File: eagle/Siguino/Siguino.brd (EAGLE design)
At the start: 71 x 39 mm, 47 parts, among them J1 FTDI, J4 10118193-0001LF, Q1 MOSFET P-CH 20V 5.3A SOT-23, U1 ATMEGA328P_TQFP, U2 LIS3MDLTR_LIS3MDLTR, U3 SPARKFUN-SENSORS_LIS3DH, U4 BME280, U5 FT232RL, U6 MAX1724EZK33+T, Y1 8MHz

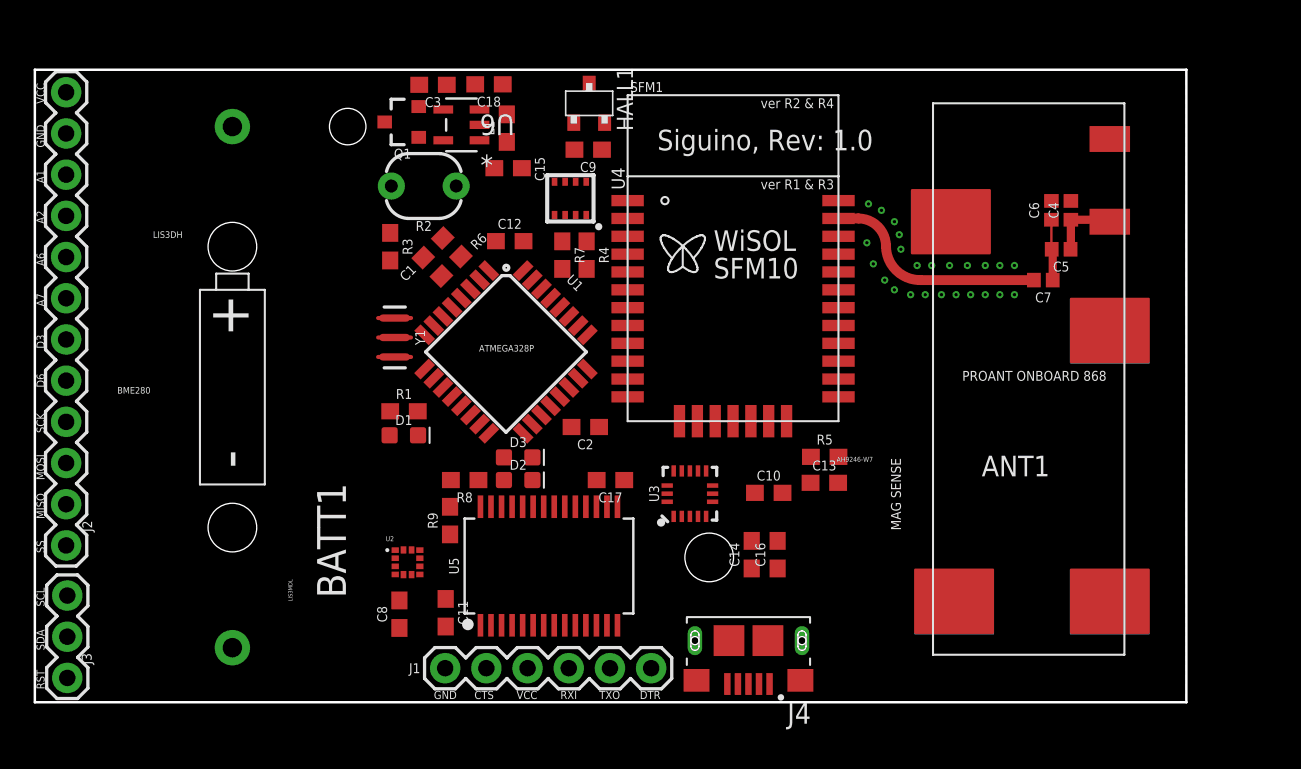
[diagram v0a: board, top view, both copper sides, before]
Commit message: Re-routed board, unfinished
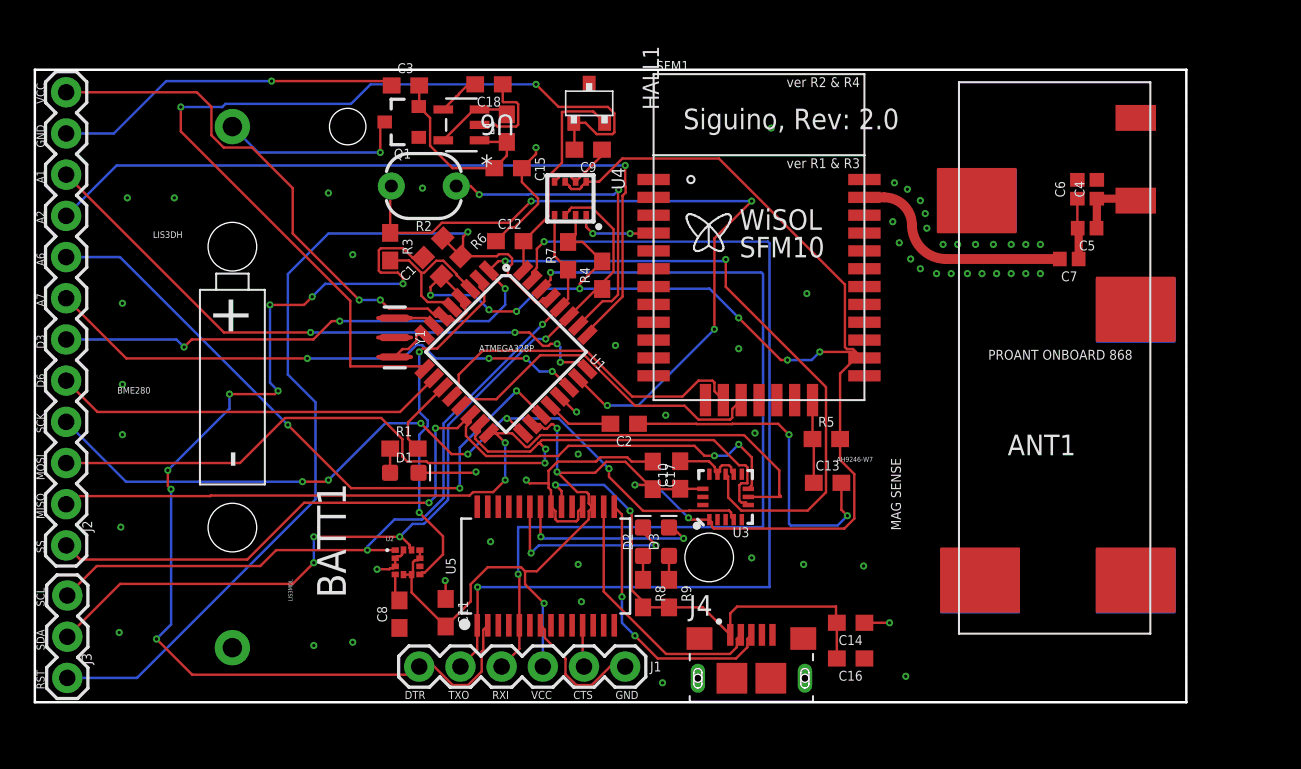
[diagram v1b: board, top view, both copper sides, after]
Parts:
- moved J1 14.3 mm to (23.7, 2.20), turned to 0 degrees
- moved R9 14.2 mm to (39.1, 6.70), turned to 270 degrees
- moved R8 13.0 mm to (37.5, 6.70), turned to 270 degrees
- moved D3 10.7 mm to (39.1, 9.90), turned to 90 degrees
- moved D2 8.59 mm to (37.5, 9.90), turned to 90 degrees
- moved C16 7.82 mm to (50.3, 2.70), turned to 180 degrees
- moved C14 7.41 mm to (50.3, 4.90), turned to 180 degrees
- moved C10 5.57 mm to (39.8, 14.0), turned to 90 degrees
- moved C17 2.63 mm to (38.1, 14.0), turned to 270 degrees
- moved C2 2.41 mm to (36.3, 17.2)
- moved J4 2.33 mm to (44.2, 1.48), turned to 0 degrees
- moved D1 2.31 mm to (22.8, 14.2)
- moved R1 2.30 mm to (22.8, 15.6)
- moved U3 2.21 mm to (42.6, 12.7)
- moved ANT1 2.06 mm to (62.9, 21.2)
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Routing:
- net VCC: track 0.00 -> 172.9 mm, vias 0 -> 14
- net GND: track 0.00 -> 112.5 mm, vias 0 -> 63
- net INT1: track 0.00 -> 71.0 mm, vias 0 -> 5
- net DTR: track 0.00 -> 65.9 mm, vias 0 -> 8
- net TXO: track 0.00 -> 61.1 mm, vias 0 -> 2
- net HALL_POWER: track 0.00 -> 58.7 mm, vias 0 -> 2
- net RESET: track 0.00 -> 57.8 mm, vias 0 -> 1
- net MOSI: track 0.00 -> 56.3 mm, vias 0 -> 2
- net SDA: track 0.00 -> 54.4 mm, vias 0 -> 4
- net RXI: track 0.00 -> 54.2 mm, vias 0 -> 2
- net SS: track 0.00 -> 54.2 mm, vias 0 -> 4
- net MISO: track 0.00 -> 53.9 mm, vias 0 -> 2
- net SCK: track 0.00 -> 50.4 mm, vias 0 -> 6
- net SCL: track 0.00 -> 48.5 mm, vias 0 -> 2
- net A2: track 0.00 -> 47.2 mm, vias 0 -> 1
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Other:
- board text added: "Siguino, Rev: 2.0"
- board text removed: "Siguino, Rev: 1.0"

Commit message: Finalised v2.0 and re-routed, gerbers created
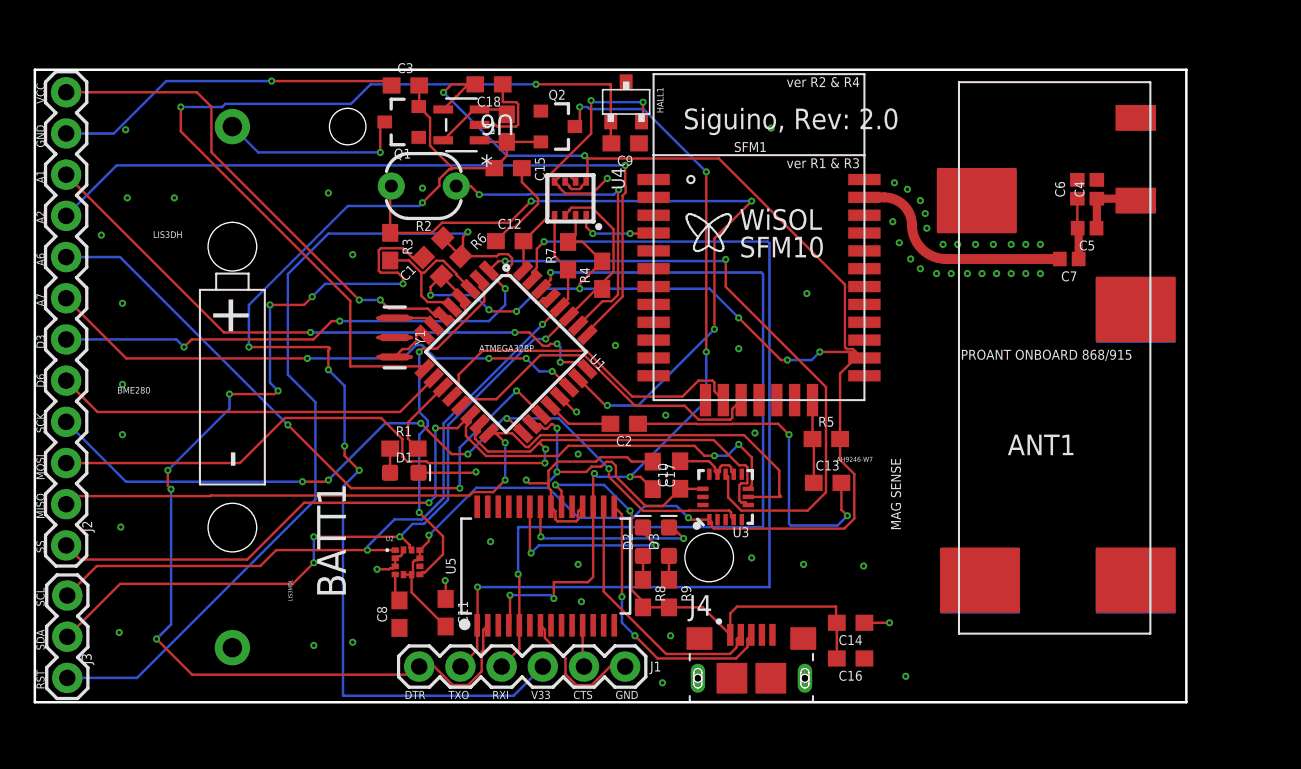
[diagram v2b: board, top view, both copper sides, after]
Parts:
- added Q2: MOSFET P-CH 20V 5.3A SOT-23, SparkFun-DiscreteSemi:SOT23-3
- ANT1: value PROOB471 -> PROOB518
- moved C9 2.31 mm to (36.4, 34.5)
- moved HALL1 2.28 mm to (36.5, 37.0)
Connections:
- removed net V33: C18.2, U6.4
- removed net VCCIO: U5.4
- new net 3V3FTDI: C17.2, Q2.3, U5.17, U5.4
- net GND: now also J4.S1, J4.S2, J4.S3, J4.S4, J4.S5, J4.S6, Q2.1
- net VBAT2: now also J1.4, Q2.2
- net VCC: now also C18.2, U6.4; no longer C17.2, J1.4, U5.17
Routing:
- net VBAT2: track 12.2 -> 74.0 mm, vias 0 -> 5
- net 3V3FTDI: track 0.00 -> 50.2 mm, vias 0 -> 7
- net VCC: track 172.9 -> 181.4 mm, vias 14 -> 15
- net HALL_POWER: track 58.7 -> 55.7 mm
- net HALL_SENSE: track 13.7 -> 16.7 mm, vias 0 -> 2
- net V33: track 2.63 -> 0.00 mm
- net GND: track 112.5 -> 112.2 mm, vias 63 -> 66
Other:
- board text added: "PROANT ONBOARD 868/915"
- board text added: "V33"
- board text removed: "PROANT ONBOARD 868"

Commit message: Fixed hatching issue on antenna pads, fixed FTDI problem
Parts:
- ANT1: device Siguino:PROANT_ONBOARD_SMD_2400 -> proant:ONBOARD_SMD_2400
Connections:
- net CTS: no longer U5.11
- net GND: now also U5.11, U5.26
- net RXI: now also U5.1; no longer U5.5
- net TXO: now also U5.5; no longer U5.1
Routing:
- net RXI: track 54.2 -> 64.9 mm
- net CTS: track 2.58 -> 0.00 mm
- net TXO: track 61.1 -> 62.4 mm
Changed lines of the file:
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@@
 <attribute name="VALUE" x="48.8" y="15.468" size="0.6096" layer="27" font="vector" ratio="20" align="top-center"/>
 </element>
-<element name="ANT1" library="Siguino" package="PROANT_ONBOARD_SMD_2400" value="PROOB518" x="62.88" y="21.23" smashed="yes">
+<element name="ANT1" library="proant" package="ONBOARD_SMD_2400" value="PROOB518" x="62.88" y="21.23" smashed="yes">
 <attribute name="NAME" x="59.98" y="15.23" size="1.27" layer="25"/>
 <attribute name="VALUE" x="59.98" y="19.03" size="1.27" layer="27"/>
@@
 <contactref element="C12" pad="1"/>
 <contactref element="C13" pad="2"/>
-<contactref element="ANT1" pad="GND"/>
 <contactref element="U3" pad="10"/>
 <contactref element="C15" pad="1"/>
@@
 <via x="5.6" y="35.3" extent="1-16" drill="0.2"/>
 <via x="4.1" y="28.8" extent="1-16" drill="0.2"/>
+<contactref element="U5" pad="26"/>
+<contactref element="U5" pad="11"/>
+<contactref element="ANT1" pad="GND"/>
 </signal>
 <signal name="VCC">
@@
 <contactref element="J1" pad="3"/>
 <contactref element="U1" pad="30"/>
-<contactref element="U5" pad="5"/>
-<wire x1="29.875" y1="4.744" x2="29.875" y2="3.295" width="0.1524" layer="1"/>
-<wire x1="29.875" y1="3.295" x2="28.78" y2="2.2" width="0.1524" layer="1"/>
 <wire x1="31.236796875" y1="25.483853125" x2="31.8" y2="26.04705625" width="0.1524" layer="1"/>
 <wire x1="31.8" y1="26.04705625" x2="31.8" y2="26.5" width="0.1524" layer="1"/>
@@
 <wire x1="44.8" y1="26.5" x2="44.9" y2="26.4" width="0.1524" layer="16"/>
 <wire x1="44.9" y1="26.4" x2="44.9" y2="10.8" width="0.1524" layer="16"/>
-<wire x1="44.9" y1="10.8" x2="29.8" y2="10.8" width="0.1524" layer="16"/>
-<wire x1="29.8" y1="10.8" x2="29.8" y2="7.9" width="0.1524" layer="16"/>
-<via x="29.8" y="7.9" extent="1-16" drill="0.2"/>
-<wire x1="29.8" y1="7.9" x2="29.875" y2="7.825" width="0.1524" layer="1"/>
-<wire x1="29.875" y1="7.825" x2="29.875" y2="4.744" width="0.1524" layer="1"/>
+<wire x1="44.9" y1="10.8" x2="28.8" y2="10.8" width="0.1524" layer="16"/>
+<wire x1="28.8" y1="10.8" x2="28.8" y2="7.9" width="0.1524" layer="16"/>
+<via x="28.8" y="7.9" extent="1-16" drill="0.2"/>
+<contactref element="U5" pad="1"/>
+<wire x1="27.275" y1="4.744" x2="27.275" y2="6.375" width="0.1524" layer="1"/>
+<wire x1="27.275" y1="6.375" x2="28.8" y2="7.9" width="0.1524" layer="1"/>
+<wire x1="26.71261875" y1="1.059" x2="25.76738125" y2="1.059" width="0.1524" layer="16"/>
+<wire x1="25.76738125" y1="1.059" x2="25.099" y2="1.72738125" width="0.1524" layer="16"/>
+<wire x1="25.099" y1="1.72738125" x2="25.099" y2="4.199" width="0.1524" layer="16"/>
+<wire x1="28.78" y1="2.2" x2="27.85361875" y2="2.2" width="0.1524" layer="16"/>
+<wire x1="27.85361875" y1="2.2" x2="26.71261875" y2="1.059" width="0.1524" layer="16"/>
+<wire x1="25.099" y1="4.199" x2="28.8" y2="7.9" width="0.1524" layer="16"/>
 </signal>
 <signal name="TXO">
 <contactref element="J1" pad="2"/>
 <contactref element="U1" pad="31"/>
-<contactref element="U5" pad="1"/>
-<wire x1="27.275" y1="4.744" x2="27.275" y2="3.235" width="0.1524" layer="1"/>
-<wire x1="27.275" y1="3.235" x2="26.24" y2="2.2" width="0.1524" layer="1"/>
 <via x="31.4" y="28.4" extent="1-16" drill="0.2"/>
 <wire x1="30.6711125" y1="26.0495375" x2="30.6711125" y2="26.501240625" width="0.1524" layer="1"/>
@@
 <wire x1="45.2" y1="28.4" x2="45.3" y2="28.3" width="0.1524" layer="16"/>
 <wire x1="45.3" y1="28.3" x2="45.3" y2="7.1" width="0.1524" layer="16"/>
-<via x="27.3" y="7.1" extent="1-16" drill="0.2"/>
-<wire x1="27.3" y1="7.1" x2="27.3" y2="4.769" width="0.1524" layer="1"/>
-<wire x1="27.3" y1="4.769" x2="27.275" y2="4.744" width="0.1524" layer="1"/>
-<wire x1="45.3" y1="7.1" x2="27.3" y2="7.1" width="0.1524" layer="16"/>
+<via x="29.9" y="7.1" extent="1-16" drill="0.2"/>
+<wire x1="45.3" y1="7.1" x2="29.9" y2="7.1" width="0.1524" layer="16"/>
+<contactref element="U5" pad="5"/>
+<wire x1="29.875" y1="4.744" x2="29.875" y2="7.075" width="0.1524" layer="1"/>
+<wire x1="29.875" y1="7.075" x2="29.9" y2="7.1" width="0.1524" layer="1"/>
+<wire x1="26.24" y1="2.2" x2="28.6" y2="4.56" width="0.1524" layer="16"/>
+<wire x1="28.6" y1="6.50274375" x2="29.19725625" y2="7.1" width="0.1524" layer="16"/>
+<wire x1="28.6" y1="4.56" x2="28.6" y2="6.50274375" width="0.1524" layer="16"/>
+<wire x1="29.19725625" y1="7.1" x2="29.9" y2="7.1" width="0.1524" layer="16"/>
 </signal>
 <signal name="DTR">
@@
 <contactref element="C5" pad="1"/>
 <contactref element="ANT1" pad="RF_FEED"/>
-<wire x1="67.6" y1="30.65" x2="67.88" y2="30.93" width="0.1524" layer="1"/>
 <contactref element="C4" pad="1"/>
-<wire x1="67.2" y1="31.05" x2="67.6" y2="30.65" width="0.1524" layer="1"/>
 <wire x1="65.46" y1="29.23" x2="65.48" y2="29.25" width="0.508" layer="1"/>
 <wire x1="65.48" y1="29.25" x2="65.48" y2="31.05" width="0.508" layer="1"/>
-<wire x1="65.48" y1="31.05" x2="67.2" y2="31.05" width="0.508" layer="1"/>
+<wire x1="67.88" y1="30.93" x2="65.6" y2="30.93" width="0.508" layer="1"/>
+<wire x1="65.6" y1="30.93" x2="65.48" y2="31.05" width="0.1524" layer="1"/>
 </signal>
 <signal name="SDA">
@@
 <signal name="CTS">
 <contactref element="J1" pad="5"/>
-<contactref element="U5" pad="11"/>
-<wire x1="33.775" y1="4.744" x2="33.775" y2="2.285" width="0.1524" layer="1"/>
-<wire x1="33.775" y1="2.285" x2="33.86" y2="2.2" width="0.1524" layer="1"/>
 </signal>
 <signal name="N$17">

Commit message: Minor updates
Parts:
- ANT1: value PROOB518 -> PRO-OB-471
- moved C5 0.40 mm to (65.3, 29.2)
- moved C6 0.40 mm to (64.7, 31.6)
- moved C7 0.40 mm to (64.2, 27.3)
- moved C4 0.40 mm to (65.9, 31.6)
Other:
- board text added: "Siguino, Rev: 2.1"
- board text removed: "Siguino, Rev: 2.0"
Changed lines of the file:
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@@
 <board>
 <plain>
-<text x="39.98" y="35.33" size="1.27" layer="21">Siguino, Rev: 2.0</text>
+<text x="39.98" y="35.33" size="1.27" layer="21">Siguino, Rev: 2.1</text>
 <wire x1="0" y1="0" x2="71" y2="0" width="0.1524" layer="20"/>
 <wire x1="71" y1="0" x2="71" y2="39" width="0.1524" layer="20"/>
@@
 <text x="51.68" y="15.13" size="0.3048" layer="21" rot="R180">AH9246-W7</text>
 <text x="67.68" y="21.73" size="0.6096" layer="21" rot="R180">PROANT ONBOARD 868/915</text>
-<text x="53.4" y="10.6" size="0.6096" layer="21" rot="R90">MAG SENSE</text>
+<text x="35.8" y="38.7" size="0.6096" layer="21" rot="R180">MAG SENSE</text>
 </plain>
 <attributes>
@@
 <attribute name="VALUE" x="24.568" y="5.52" size="0.6096" layer="27" font="vector" ratio="20" rot="R270" align="top-center"/>
 </element>
-<element name="C5" library="SparkFun-Capacitors" package="0402" value="2.2pF" x="64.88" y="29.23" smashed="yes" rot="R180">
-<attribute name="NAME" x="64.88" y="28.468" size="0.6096" layer="25" font="vector" ratio="20" rot="R180" align="bottom-center"/>
-<attribute name="PROD_ID" value="CAP-13456" x="64.88" y="29.23" size="1.778" layer="27" rot="R180" display="off"/>
-<attribute name="VALUE" x="64.88" y="29.992" size="0.6096" layer="27" font="vector" ratio="20" rot="R180" align="top-center"/>
-</element>
-<element name="C7" library="SparkFun-Resistors" package="0402" value=" 0 OHM" x="63.78" y="27.33" smashed="yes" rot="R180">
-<attribute name="NAME" x="63.78" y="26.568" size="0.6096" layer="25" font="vector" ratio="20" rot="R180" align="bottom-center"/>
-<attribute name="PROD_ID" value=" " x="63.78" y="27.33" size="1.778" layer="27" rot="R180" display="off"/>
-<attribute name="VALUE" x="63.78" y="28.092" size="0.6096" layer="27" font="vector" ratio="20" rot="R180" align="top-center"/>
+<element name="C5" library="SparkFun-Capacitors" package="0402" value="2.2pF" x="65.28" y="29.23" smashed="yes" rot="R180">
+<attribute name="NAME" x="65.28" y="28.468" size="0.6096" layer="25" font="vector" ratio="20" rot="R180" align="bottom-center"/>
+<attribute name="PROD_ID" value="CAP-13456" x="65.28" y="29.23" size="1.778" layer="27" rot="R180" display="off"/>
+<attribute name="VALUE" x="65.28" y="29.992" size="0.6096" layer="27" font="vector" ratio="20" rot="R180" align="top-center"/>
+</element>
+<element name="C7" library="SparkFun-Resistors" package="0402" value=" 0 OHM" x="64.18" y="27.33" smashed="yes" rot="R180">
+<attribute name="NAME" x="64.18" y="26.568" size="0.6096" layer="25" font="vector" ratio="20" rot="R180" align="bottom-center"/>
+<attribute name="PROD_ID" value=" " x="64.18" y="27.33" size="1.778" layer="27" rot="R180" display="off"/>
+<attribute name="VALUE" x="64.18" y="28.092" size="0.6096" layer="27" font="vector" ratio="20" rot="R180" align="top-center"/>
 </element>
 <element name="J3" library="SparkFun-Connectors" package="1X03" value="" x="2" y="1.5" smashed="yes" rot="R90">
@@
 <attribute name="VALUE" x="48.8" y="15.468" size="0.6096" layer="27" font="vector" ratio="20" align="top-center"/>
 </element>
-<element name="ANT1" library="proant" package="ONBOARD_SMD_2400" value="PROOB518" x="62.88" y="21.23" smashed="yes">
+<element name="ANT1" library="proant" package="ONBOARD_SMD_2400" value="PRO-OB-471" x="62.88" y="21.23" smashed="yes">
 <attribute name="NAME" x="59.98" y="15.23" size="1.27" layer="25"/>
-<attribute name="VALUE" x="59.98" y="19.03" size="1.27" layer="27"/>
+<attribute name="VALUE" x="57.58" y="19.03" size="1.27" layer="27"/>
 </element>
 <element name="R6" library="SparkFun-Resistors" package="0603" value="10k" x="25.67" y="26.88" smashed="yes" rot="R225">
@@
 <attribute name="VALUE" x="27.508" y="32.78" size="0.6096" layer="27" font="vector" ratio="20" rot="R270" align="top-center"/>
 </element>
-<element name="C6" library="SparkFun-Capacitors" package="0402" value="0.7pF" x="64.28" y="31.63" smashed="yes" rot="R90">
-<attribute name="NAME" x="63.518" y="31.63" size="0.6096" layer="25" font="vector" ratio="20" rot="R90" align="bottom-center"/>
-<attribute name="PROD_ID" value="CAP-13456" x="64.28" y="31.63" size="1.778" layer="27" rot="R90" display="off"/>
-<attribute name="VALUE" x="65.042" y="31.63" size="0.6096" layer="27" font="vector" ratio="20" rot="R90" align="top-center"/>
-</element>
-<element name="C4" library="SparkFun-Capacitors" package="0402" value="0.6pF" x="65.48" y="31.63" smashed="yes" rot="R90">
-<attribute name="NAME" x="64.718" y="31.63" size="0.6096" layer="25" font="vector" ratio="20" rot="R90" align="bottom-center"/>
-<attribute name="PROD_ID" value="CAP-13456" x="65.48" y="31.63" size="1.778" layer="27" rot="R90" display="off"/>
-<attribute name="VALUE" x="66.242" y="31.63" size="0.6096" layer="27" font="vector" ratio="20" rot="R90" align="top-center"/>
+<element name="C6" library="SparkFun-Capacitors" package="0402" value="0.7pF" x="64.68" y="31.63" smashed="yes" rot="R90">
+<attribute name="NAME" x="63.918" y="31.63" size="0.6096" layer="25" font="vector" ratio="20" rot="R90" align="bottom-center"/>
+<attribute name="PROD_ID" value="CAP-13456" x="64.68" y="31.63" size="1.778" layer="27" rot="R90" display="off"/>
+<attribute name="VALUE" x="65.442" y="31.63" size="0.6096" layer="27" font="vector" ratio="20" rot="R90" align="top-center"/>
+</element>
+<element name="C4" library="SparkFun-Capacitors" package="0402" value="0.6pF" x="65.88" y="31.63" smashed="yes" rot="R90">
+<attribute name="NAME" x="65.118" y="31.63" size="0.6096" layer="25" font="vector" ratio="20" rot="R90" align="bottom-center"/>
+<attribute name="PROD_ID" value="CAP-13456" x="65.88" y="31.63" size="1.778" layer="27" rot="R90" display="off"/>
+<attribute name="VALUE" x="66.642" y="31.63" size="0.6096" layer="27" font="vector" ratio="20" rot="R90" align="top-center"/>
 </element>
 <element name="BATT1" library="Siguino" package="SPARKFUN-BATTERIES_BATTERYHOLDER-CR2" value="SPARKFUN-BATTERIES_CR2-BATTERY-HOLDERPTH" x="12.18" y="19.43" smashed="yes" rot="R90">
@@
 <contactref element="ANT1" pad="RF_FEED"/>
 <contactref element="C4" pad="1"/>
-<wire x1="65.46" y1="29.23" x2="65.48" y2="29.25" width="0.508" layer="1"/>
-<wire x1="65.48" y1="29.25" x2="65.48" y2="31.05" width="0.508" layer="1"/>
-<wire x1="67.88" y1="30.93" x2="65.6" y2="30.93" width="0.508" layer="1"/>
-<wire x1="65.6" y1="30.93" x2="65.48" y2="31.05" width="0.1524" layer="1"/>
+<wire x1="65.86" y1="29.23" x2="65.88" y2="29.25" width="0.508" layer="1" curve="90"/>
+<wire x1="65.88" y1="29.25" x2="65.88" y2="31.05" width="0.508" layer="1"/>
+<wire x1="65.88" y1="31.05" x2="66" y2="30.93" width="0.508" layer="1" curve="90"/>
+<wire x1="66" y1="30.93" x2="67.88" y2="30.93" width="0.508" layer="1"/>
 </signal>
 <signal name="SDA">
@@
 <contactref element="C7" pad="1"/>
 <contactref element="C6" pad="1"/>
-<wire x1="64.28" y1="31.05" x2="64.28" y2="29.25" width="0.1524" layer="1"/>
-<wire x1="64.28" y1="29.25" x2="64.3" y2="29.23" width="0.1524" layer="1"/>
-<wire x1="64.3" y1="29.23" x2="64.36" y2="29.17" width="0.508" layer="1"/>
-<wire x1="64.36" y1="29.17" x2="64.36" y2="27.33" width="0.508" layer="1"/>
+<wire x1="64.76" y1="27.33" x2="64.7" y2="27.39" width="0.508" layer="1" curve="-90"/>
+<wire x1="64.7" y1="27.39" x2="64.7" y2="29.23" width="0.508" layer="1"/>
+<wire x1="64.7" y1="29.23" x2="64.68" y2="29.25" width="0.508" layer="1" curve="-90"/>
+<wire x1="64.68" y1="29.25" x2="64.68" y2="31.05" width="0.508" layer="1"/>
 </signal>
 <signal name="VBAT">
@@
 <wire x1="52.38" y1="31.13" x2="54.08" y2="29.43" width="0.6096" layer="1" curve="-90"/>
 <wire x1="54.08" y1="29.43" x2="56.18" y2="27.33" width="0.6096" layer="1" curve="90"/>
-<wire x1="56.18" y1="27.33" x2="63.2" y2="27.33" width="0.6096" layer="1"/>
+<wire x1="56.18" y1="27.33" x2="63.6" y2="27.33" width="0.6096" layer="1"/>
 <wire x1="51.15" y1="31.13" x2="52.38" y2="31.13" width="0.6096" layer="1"/>
 </signal>
